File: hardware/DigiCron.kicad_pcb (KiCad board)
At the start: 2 copper layers, 36 x 36 mm, 45 parts, among them J100 Solder pad, J101 Solder pad, J102 Solder pad, J103 Solder pad, J200 Conn_Receptacle_2P, Q100 BSS138, Q101 AO3400A, Q200 AO3401A, SW200 SW_Push_Dual, SW201 SW_Push_Dual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

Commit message: Add programming pins to PCB
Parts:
- added J201: Solder pad, TestPoint:TestPoint_Pad_2.0x2.0mm, B.Cu at (212.1, 67.5)
- added J202: Solder pad, TestPoint:TestPoint_Pad_2.0x2.0mm, B.Cu at (206.5, 67.5)
- added J203: Solder pad, TestPoint:TestPoint_Pad_2.0x2.0mm, B.Cu at (200.8, 67.5)
- added J204: Solder pad, TestPoint:TestPoint_Pad_2.0x2.0mm, B.Cu at (195.1, 67.5)
- added R209: 22, Resistor_SMD:R_0201_0603Metric_Pad0.64x0.40mm_HandSolder, B.Cu at (199.6, 100.0)
- added R210: 22, Resistor_SMD:R_0201_0603Metric_Pad0.64x0.40mm_HandSolder, B.Cu at (199.6, 101.0)
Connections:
- X200 pad A6: USB_D+ -> Net-(R209-Pad2)
- X200 pad A7: USB_D- -> Net-(R210-Pad2)
- X200 pad B6: USB_D+ -> Net-(R209-Pad2)
- X200 pad B7: USB_D- -> Net-(R210-Pad2)
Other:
- board text added: "3V3"
- board text added: "CLK"
- board text added: "DIO"
- board text added: "G"

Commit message: Add crystal oscillator and hide designators from PCB
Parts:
- added C206: 25p, Capacitor_SMD:C_0201_0603Metric_Pad0.64x0.40mm_HandSolder, B.Cu at (180.6, 75.5)
- added C207: 25p, Capacitor_SMD:C_0201_0603Metric_Pad0.64x0.40mm_HandSolder, B.Cu at (180.6, 73.5)
- added XTAL200: ECX-.327-CDX-1293, ECX-.327-CDX-1293:XTAL_ECS-.327-12.5-34RR-TR, B.Cu at (182.6, 75.5)
- moved U105 2.53 mm to (185.6, 73.5)
- moved C202 1.16 mm to (191.6, 88.0)
- moved U202 1.00 mm to (182.5, 88.0)
- moved C205 0.85 mm to (181.1, 85.0), turned to -90 degrees
- moved R208 0.59 mm to (185.1, 88.4)
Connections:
- U100 pad 17: unconnected-(U100-XL1/P0.00-Pad17) -> XL1
- U100 pad 18: unconnected-(U100-XL2/P0.01-Pad18) -> XL2

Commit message: Perform PCB routing (WIP)
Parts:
- removed U103: LTR-390UV-01, LTR390:SMD6_LTR-390UV-01_LTO
- added R104: 10K, Capacitor_SMD:C_0201_0603Metric_Pad0.64x0.40mm_HandSolder, B.Cu at (201.6, 78.5)
- moved C207 4.68 mm to (181.7, 78.0), turned to 180 degrees
- moved C206 2.64 mm to (181.7, 73.0), turned to 180 degrees
- moved R209 1.37 mm to (200.6, 101.0)
- moved R210 1.37 mm to (200.6, 100.0)
- moved C202 1.18 mm to (192.1, 87.0), turned to 90 degrees
- moved C201 0.92 mm to (199.0, 83.9), turned to 90 degrees
- moved R200 0.75 mm to (205.1, 87.0)
- moved R203 0.72 mm to (198.0, 86.9)
- moved C203 0.71 mm to (185.6, 84.2)
- moved C204 0.66 mm to (186.5, 84.2)
- moved R201 0.57 mm to (208.6, 82.0)
- moved R208 0.52 mm to (185.1, 89.0)
- moved C200 0.50 mm to (204.1, 87.0)
- moved D200 0.50 mm to (202.1, 86.0)
- moved R101 0.35 mm to (200.1, 78.5)
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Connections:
- U100 pad 10: VDIV -> SDA
- U100 pad 12: AREF -> 5V_EN
- U100 pad 13: A3 -> unconnected-(U100-P0.28/AIN4-Pad13)
- U100 pad 14: A2 -> SCL
- U100 pad 16: unconnected-(U100-P0.27-Pad16) -> VDIV
- U100 pad 21: A1 -> unconnected-(U100-P0.05/AIN3-Pad21)
- U100 pad 24: IR_IN -> unconnected-(U100-P0.08-Pad24)
- U100 pad 27: SCL -> unconnected-(U100-TRACEDATA2/P0.11-Pad27)
- U100 pad 29: SDA -> unconnected-(U100-TRACEDATA1/P0.12-Pad29)
- U100 pad 36: SCK -> unconnected-(U100-P0.14-Pad36)
- U100 pad 37: MOSI -> unconnected-(U100-P0.13-Pad37)
- U100 pad 39: MISO -> unconnected-(U100-P0.15-Pad39)
- U100 pad 4: 5V_EN -> unconnected-(U100-P1.11-Pad4)
- U100 pad 41: QSPI_D0 -> unconnected-(U100-P0.17-Pad41)
- U100 pad 42: QSPI_SCK -> unconnected-(U100-P0.19-Pad42)
- U100 pad 43: QSPI_D3 -> unconnected-(U100-P0.21-Pad43)
- U100 pad 45: QSPI_D2 -> unconnected-(U100-P0.23-Pad45)
- U100 pad 46: QSPI_D1 -> unconnected-(U100-P0.22-Pad46)
- U100 pad 47: ADPS_IRQ -> unconnected-(U100-TRACEDATA0/P1.00-Pad47)
- U100 pad 48: RXD -> unconnected-(U100-P0.24-Pad48)
- U100 pad 49: TXD -> unconnected-(U100-P0.25-Pad49)
- U104 pad 12: +3V3 -> GND
- U105 pad 2: unconnected-(U105-CSB-Pad2) -> +3V3
- U105 pad 5: unconnected-(U105-SDO-Pad5) -> +3V3
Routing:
- net GND: track 0.00 -> 132.9 mm, vias 0 -> 29
- net +3V3: track 0.00 -> 96.1 mm, vias 0 -> 12
- net SWCLK: track 0.00 -> 83.3 mm, vias 0 -> 2
- net HCMS_RS: track 0.00 -> 79.6 mm, vias 0 -> 1
- net +5V: track 0.00 -> 78.2 mm, vias 0 -> 2
- net SWDIO: track 0.00 -> 74.0 mm, vias 0 -> 2
- net VBAT: track 0.00 -> 70.5 mm, vias 0 -> 3
- net VBUS: track 0.00 -> 69.3 mm, vias 0 -> 7
- net HCMS_BLANK: track 0.00 -> 66.2 mm, vias 0 -> 1
- net HCMS_DATA_IN: track 0.00 -> 62.0 mm, vias 0 -> 2
- net HCMS_CLOCK: track 0.00 -> 47.3 mm, vias 0 -> 3
- net HCMS_RESET: track 0.00 -> 45.7 mm, vias 0 -> 2
- net PIEZO_A: track 0.00 -> 44.4 mm
- net HCMS_DATA_SHARE: track 0.00 -> 41.6 mm
- net VIBMOTOR: track 0.00 -> 41.2 mm, vias 0 -> 2
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- added copper zone on F.Cu, net GND

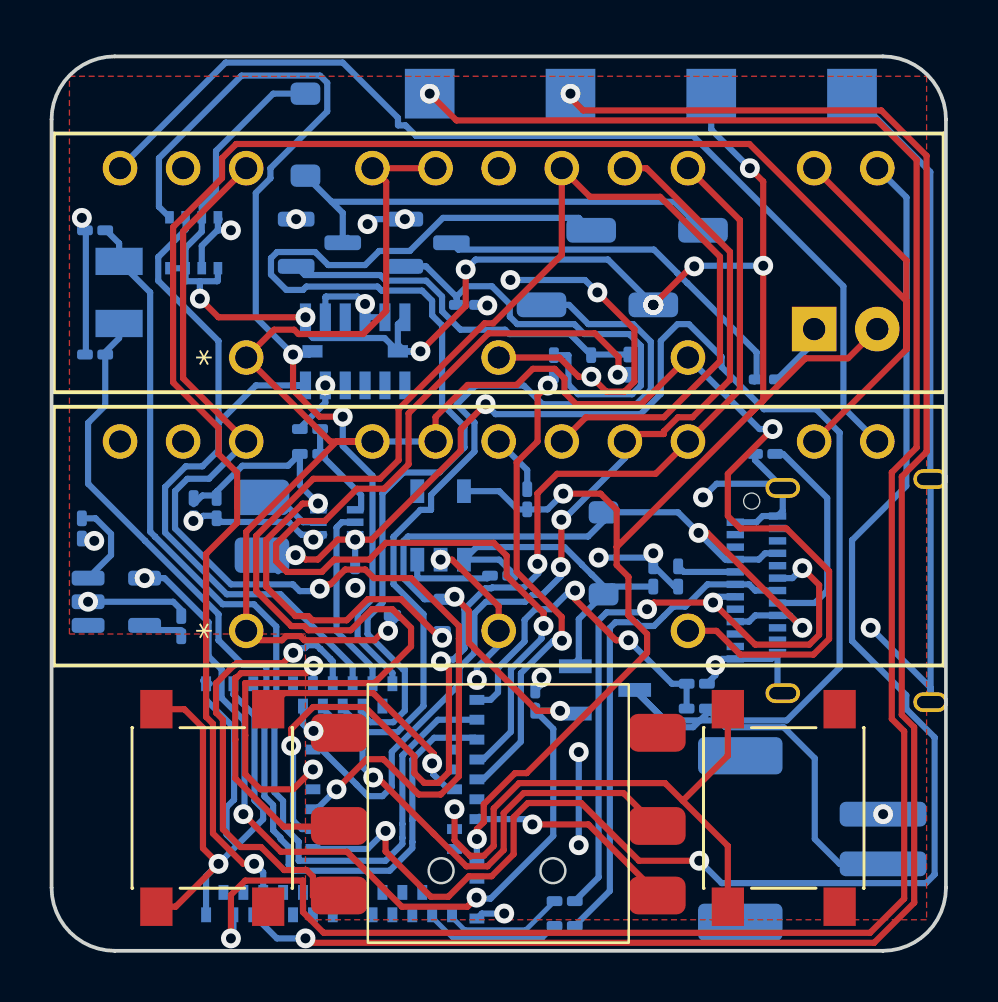
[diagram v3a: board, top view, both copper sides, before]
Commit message: Clean up some VBAT traces
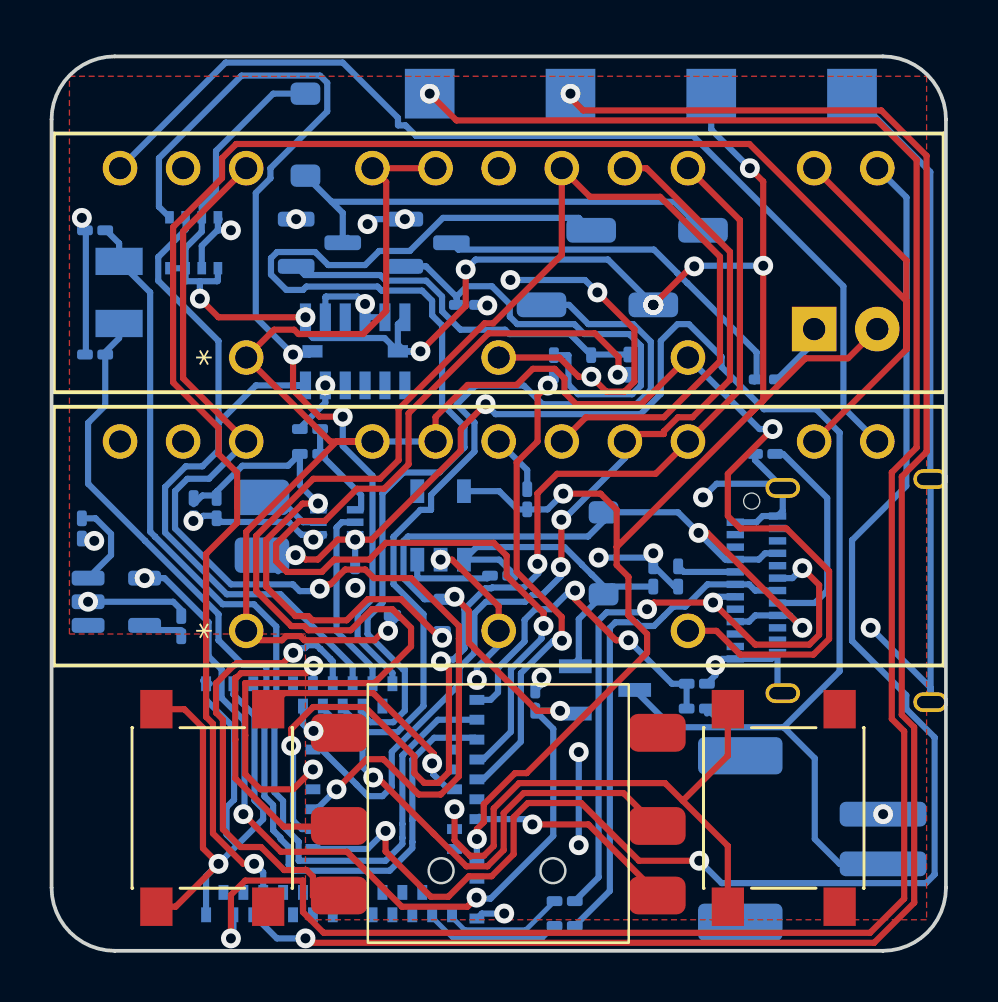
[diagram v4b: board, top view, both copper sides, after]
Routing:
- net VBAT: track 70.5 -> 64.7 mm
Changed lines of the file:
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@@
 	)
 	(segment
-		(start 203.6032 80.441)
-		(end 197.771 80.441)
+		(start 209.368 93.04)
+		(end 210.62 94.292)
 		(width 0.25)
 		(layer "B.Cu")
@@
 	)
 	(segment
-		(start 205.727499 93.04)
-		(end 204.87 93.04)
+		(start 211.62 81.185758)
+		(end 211.62 90.788)
 		(width 0.25)
 		(layer "B.Cu")
@@
 	)
 	(segment
-		(start 209.368 93.04)
-		(end 210.62 94.292)
+		(start 203.37 91.54)
+		(end 204.87 93.04)
 		(width 0.25)
 		(layer "B.Cu")
@@
 	)
 	(segment
-		(start 211.62 90.636008)
-		(end 211.62 81.185758)
-		(width 0.25)
-		(layer "B.Cu")
-		(net 82)
-	)
-	(segment
-		(start 205.550242 76.816)
-		(end 205.094804 76.816)
-		(width 0.25)
-		(layer "B.Cu")
-		(net 82)
-	)
-	(segment
-		(start 206.87 78.54)
-		(end 206.87 78.135758)
+		(start 204.87 93.04)
+		(end 207.0275 93.04)
 		(width 0.25)
 		(layer "B.Cu")
@@
 	)
 	(segment
-		(start 204.422 77.488804)
-		(end 204.422 79.6222)
-		(width 0.25)
-		(layer "B.Cu")
-		(net 82)
-	)
-	(segment
-		(start 197.771 80.441)
-		(end 197.37 80.04)
-		(width 0.25)
-		(layer "B.Cu")
-		(net 82)
-	)
-	(segment
-		(start 206.2775 92.489999)
-		(end 205.727499 93.04)
+		(start 206.87 78.54)
+		(end 208.573405 80.243405)
 		(width 0.25)
 		(layer "B.Cu")
@@
 	)
 	(segment
-		(start 204.422 79.6222)
-		(end 203.6032 80.441)
+		(start 205.550242 76.816)
+		(end 206.87 78.135758)
 		(width 0.25)
 		(layer "B.Cu")
@@
 	)
 	(segment
-		(start 210.677647 80.243405)
-		(end 208.573405 80.243405)
+		(start 208.573405 80.243405)
+		(end 210.677647 80.243405)
 		(width 0.25)
 		(layer "B.Cu")
@@
 	)
 	(segment
-		(start 209.490008 92.766)
-		(end 211.62 90.636008)
+		(start 203.6032 80.441)
+		(end 204.422 79.6222)
+		(width 0.25)
+		(layer "B.Cu")
+		(net 82)
+	)
+	(segment
+		(start 204.422 77.488804)
+		(end 205.094804 76.816)
+		(width 0.25)
+		(layer "B.Cu")
+		(net 82)
+	)
+	(segment
+		(start 206.87 78.135758)
+		(end 206.87 78.54)
 		(width 0.25)
 		(layer "B.Cu")
@@
 		(start 211.62 98.54)
 		(end 213.37 98.54)
+		(width 0.25)
+		(layer "B.Cu")
+		(net 82)
+	)
+	(segment
+		(start 210.677647 80.243405)
+		(end 211.62 81.185758)
 		(width 0.25)
 		(layer "B.Cu")
@@
 	)
 	(segment
-		(start 208.573405 80.243405)
-		(end 206.87 78.54)
-		(width 0.25)
-		(layer "B.Cu")
-		(net 82)
-	)
-	(segment
-		(start 203.37 91.54)
-		(end 204.596 92.766)
-		(width 0.25)
-		(layer "B.Cu")
-		(net 82)
-	)
-	(segment
 		(start 210.62 94.292)
 		(end 210.62 97.54)
@@
 	(segment
 		(start 205.094804 76.816)
-		(end 204.422 77.488804)
+		(end 205.550242 76.816)
 		(width 0.25)
 		(layer "B.Cu")
@@
 	)
 	(segment
-		(start 204.87 93.04)
-		(end 203.37 91.54)
+		(start 197.771 80.441)
+		(end 203.6032 80.441)
 		(width 0.25)
 		(layer "B.Cu")
@@
 	)
 	(segment
-		(start 204.596 92.766)
-		(end 209.490008 92.766)
+		(start 197.37 80.04)
+		(end 197.771 80.441)
 		(width 0.25)
 		(layer "B.Cu")
@@
 	)
 	(segment
-		(start 206.87 78.135758)
-		(end 205.550242 76.816)
+		(start 204.422 79.6222)
+		(end 204.422 77.488804)
 		(width 0.25)
 		(layer "B.Cu")
@@
 	)
 	(segment
-		(start 211.62 81.185758)
-		(end 210.677647 80.243405)
+		(start 211.62 90.788)
+		(end 209.368 93.04)
 		(width 0.25)
 		(layer "B.Cu")

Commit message: Finish routing of PCB
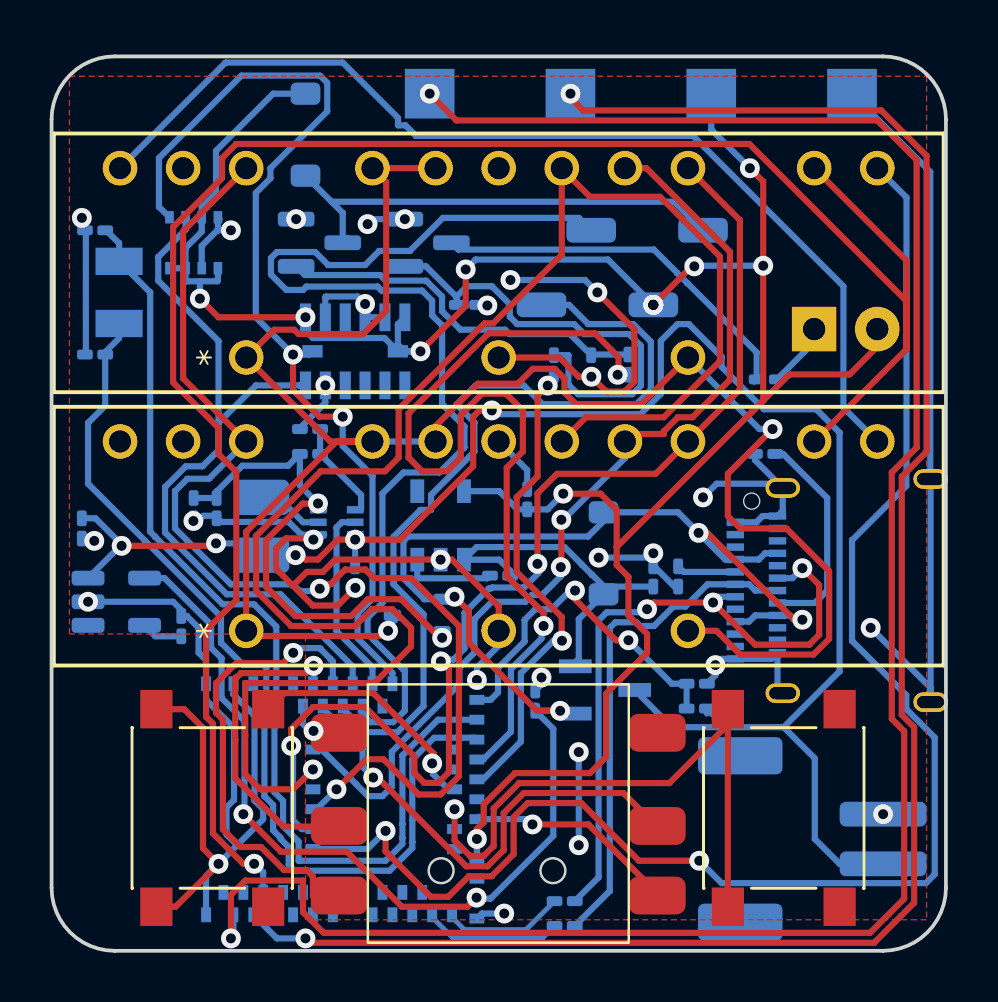
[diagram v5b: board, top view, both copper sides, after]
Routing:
- net GND: track 132.9 -> 148.9 mm
- net VBAT: track 64.7 -> 71.5 mm, vias 3 -> 5
- net VIBMOTOR: track 41.2 -> 36.9 mm
- net +3V3: track 96.1 -> 98.0 mm
- net JOY_HOME: track 22.6 -> 24.2 mm
- net VBUS: track 69.3 -> 69.0 mm, vias 7 -> 6

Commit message: Check over PCB design and re-add LTR390
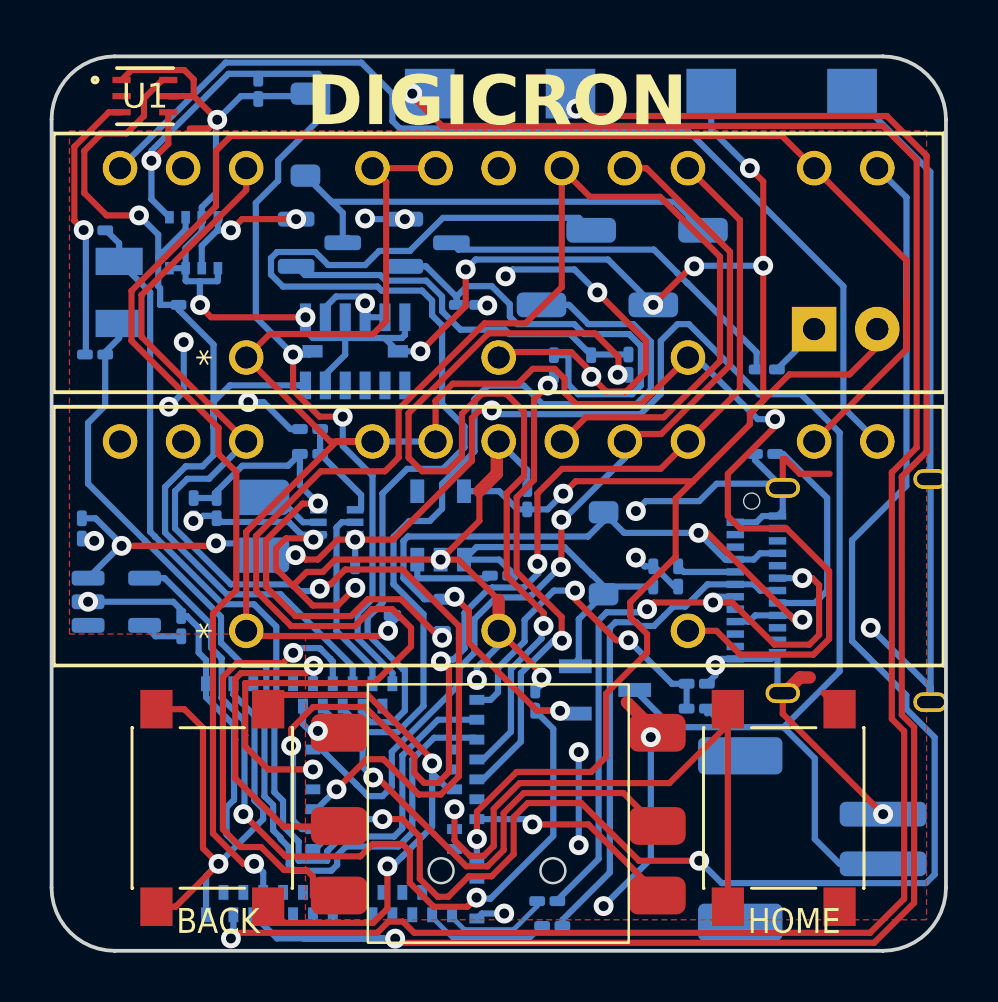
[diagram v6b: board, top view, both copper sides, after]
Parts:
- added R106: 10K, Capacitor_SMD:C_0201_0603Metric_Pad0.64x0.40mm_HandSolder, B.Cu at (185.4, 76.0)
- added R107: 10K, Capacitor_SMD:C_0201_0603Metric_Pad0.64x0.40mm_HandSolder, B.Cu at (188.2, 67.3)
- added U1: LTR-390UV-01, LTR390:SMD6_LTR-390UV-01_LTO, F.Cu at (183.7, 67.6)
- moved R210 0.70 mm to (199.9, 100.0)
- moved R209 0.50 mm to (200.1, 101.0)
- moved R100 0.40 mm to (208.7, 78.6)
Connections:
- U104 pad 12: GND -> +3V3
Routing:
- net GND: track 148.9 -> 192.8 mm, vias 29 -> 32
- net SDA: track 30.3 -> 42.5 mm, vias 0 -> 1
- net +3V3: track 98.0 -> 109.9 mm, vias 12 -> 11
- net JOY_BACK: track 9.94 -> 21.7 mm, vias 1 -> 2
- net HCMS_RS: track 79.6 -> 75.4 mm
- net SCL: track 40.5 -> 43.4 mm, vias 2 -> 3
- net SWDIO: track 73.9 -> 76.5 mm
- net SWCLK: track 83.3 -> 81.1 mm
- net VBUS: track 69.0 -> 70.8 mm
- net HCMS_RESET: track 45.7 -> 47.1 mm
- net +5V: track 77.7 -> 78.7 mm
- net HCMS_CE: track 39.4 -> 38.4 mm
- net HCMS_DATA_IN: track 62.0 -> 62.9 mm
- net PIEZO_B: track 34.4 -> 33.7 mm
- net USB_D-: track 4.91 -> 4.33 mm
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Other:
- board text added: "BACK"
- board text added: "DIGICRON"
- board text added: "HOME"
